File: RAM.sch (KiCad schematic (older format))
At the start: 3 parts, among them U2 MT41K64M16TW-107_AAT_J_TR

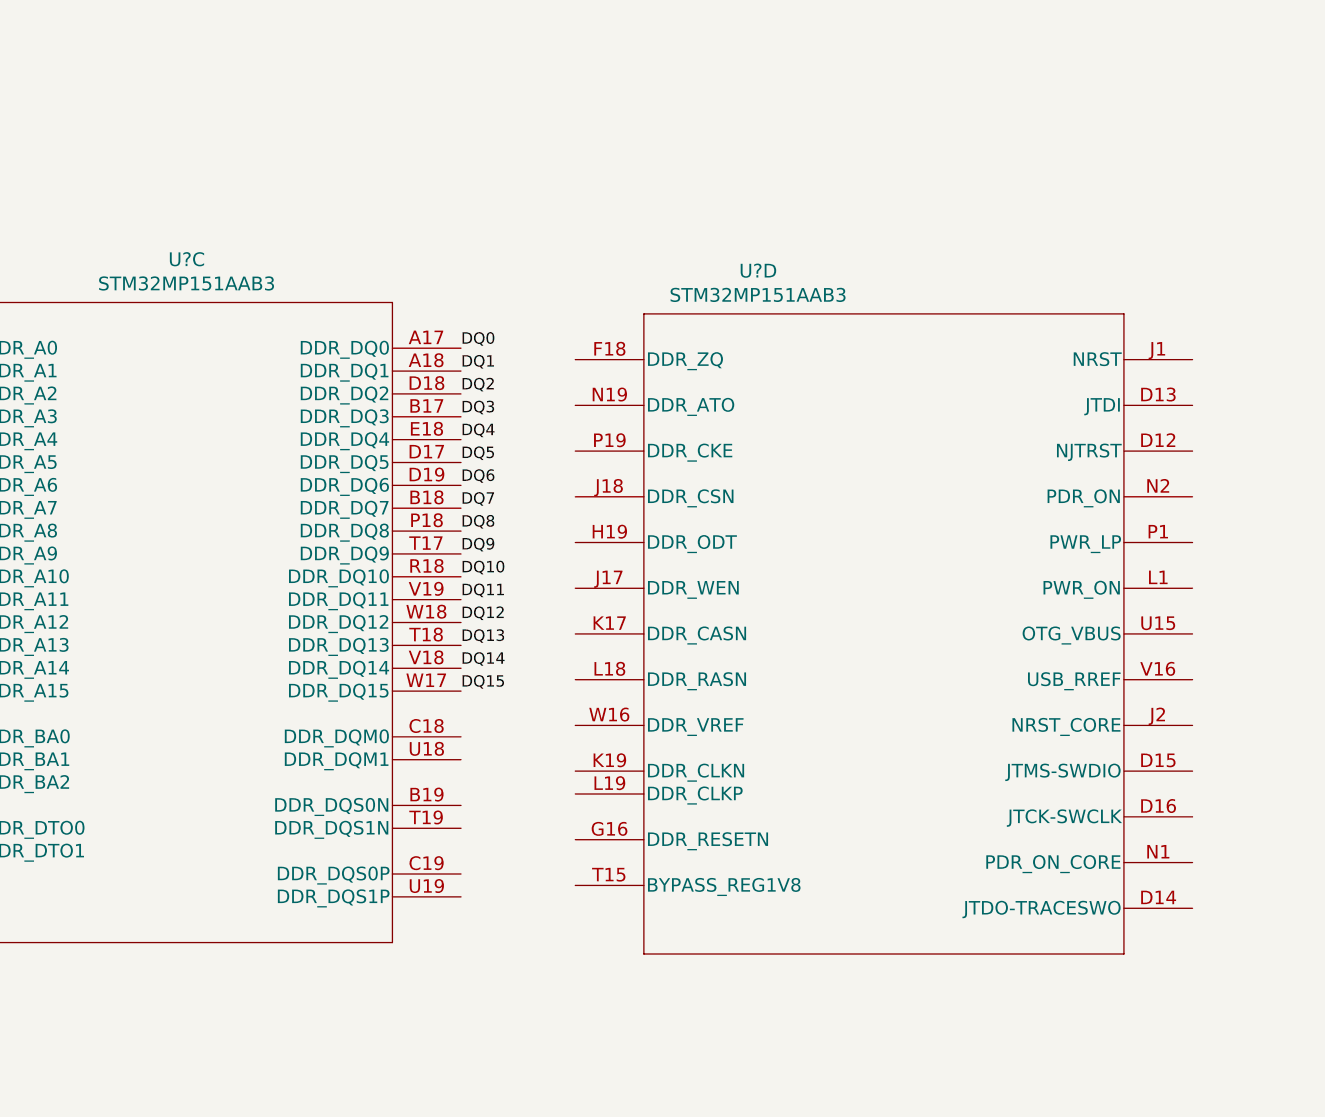
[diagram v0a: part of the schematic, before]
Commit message: Add bulk labels for RAM and ethernet
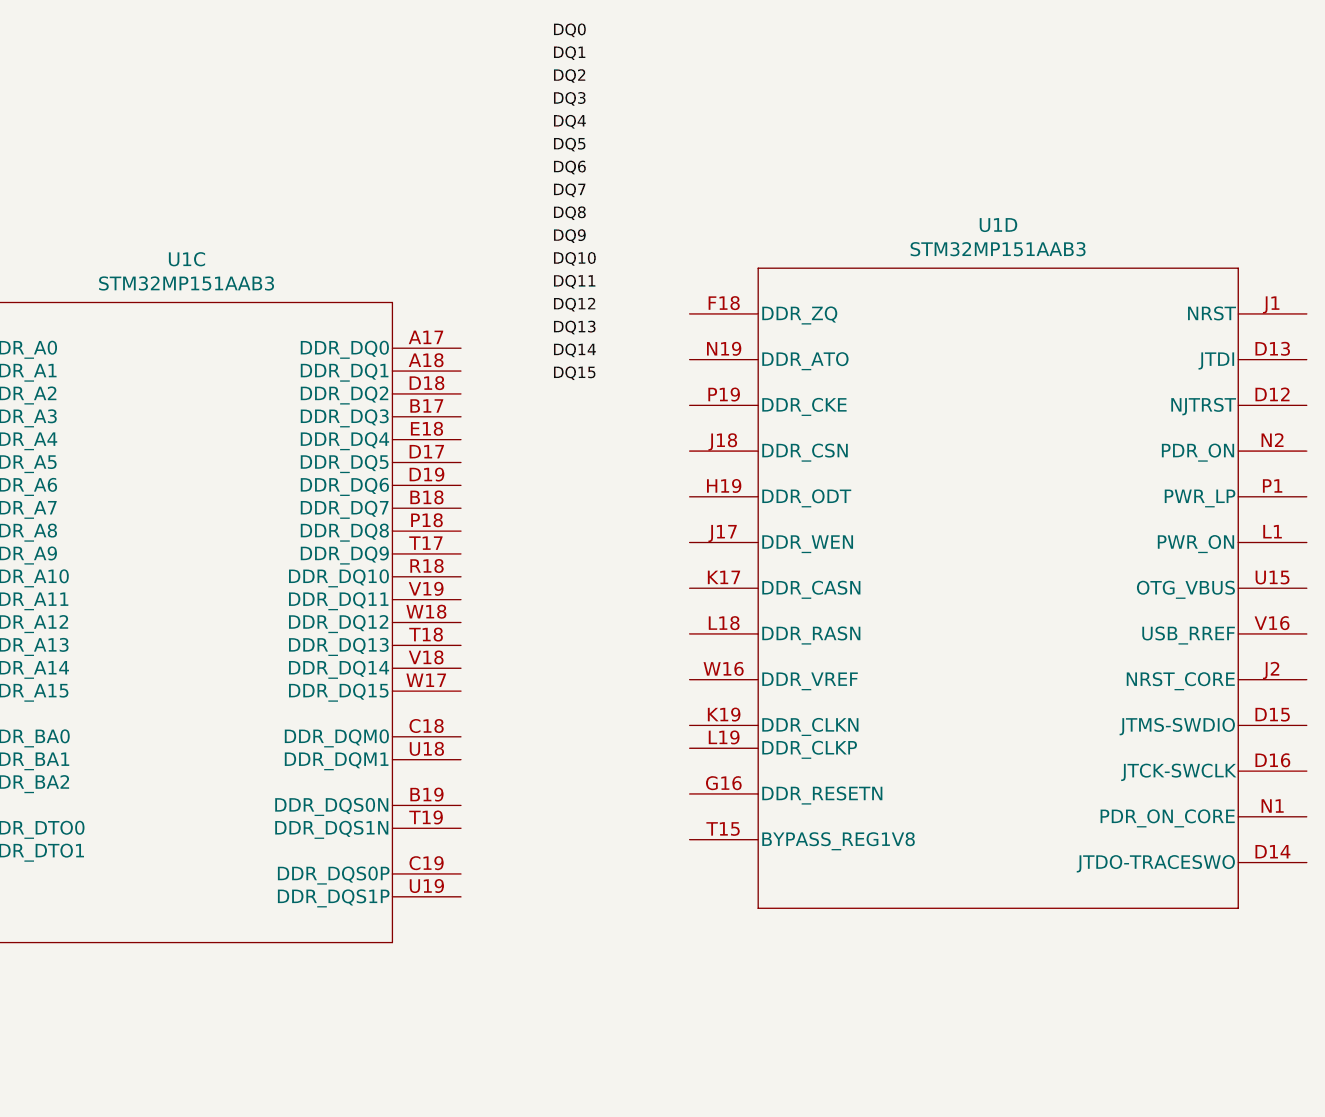
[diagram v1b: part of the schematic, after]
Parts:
- gave numbers to parts that had none: 1
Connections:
- net DQ0: no longer U1.A17 (DDR_DQ0)
- net DQ1: no longer U1.A18 (DDR_DQ1)
- net DQ10: no longer U1.R18 (DDR_DQ10)
- net DQ11: no longer U1.V19 (DDR_DQ11)
- net DQ12: no longer U1.W18 (DDR_DQ12)
- net DQ13: no longer U1.T18 (DDR_DQ13)
- net DQ14: no longer U1.V18 (DDR_DQ14)
- net DQ15: no longer U1.W17 (DDR_DQ15)
- net DQ2: no longer U1.D18 (DDR_DQ2)
- net DQ3: no longer U1.B17 (DDR_DQ3)
- net DQ4: no longer U1.E18 (DDR_DQ4)
- net DQ5: no longer U1.D17 (DDR_DQ5)
- net DQ6: no longer U1.D19 (DDR_DQ6)
- net DQ7: no longer U1.B18 (DDR_DQ7)
- net DQ8: no longer U1.P18 (DDR_DQ8)
- net DQ9: no longer U1.T17 (DDR_DQ9)
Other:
- moved on the sheet: U1D
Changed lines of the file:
@@
 L LinuxBoard:STM32MP151AAB3 U?
 U 4 1 6049E2E1
-P 7350 1450
+P 7850 1250
 AR Path="/601728E9/6049E2E1" Ref="U?"  Part="4"
-AR Path="/60172A77/6049E2E1" Ref="U?"  Part="4"
-F 0 "U?" H 8650 1837 60  0000 C CNN
-F 1 "STM32MP151AAB3" H 8650 1731 60  0000 C CNN
-F 2 "LinuxBoard:STM32MP151AAB3" H 8350 1690 60  0001 C CNN
-F 3 "" H 7350 1450 60  0000 C CNN
-	4    7350 1450
+AR Path="/60172A77/6049E2E1" Ref="U1"  Part="4"
+F 0 "U1" H 9700 1637 60  0000 C CNN
+F 1 "STM32MP151AAB3" H 9700 1531 60  0000 C CNN
+F 2 "LinuxBoard:STM32MP151AAB3" H 8850 1490 60  0001 C CNN
+F 3 "" H 7850 1250 60  0000 C CNN
+	4    7850 1250
 	1    0    0    -1
 $EndComp
@@
 P 4950 1400
 AR Path="/601728E9/6049E2E7" Ref="U?"  Part="3"
-AR Path="/60172A77/6049E2E7" Ref="U?"  Part="3"
-F 0 "U?" H 6150 1787 60  0000 C CNN
+AR Path="/60172A77/6049E2E7" Ref="U1"  Part="3"
+F 0 "U1" H 6150 1787 60  0000 C CNN
 F 1 "STM32MP151AAB3" H 6150 1681 60  0000 C CNN
 F 2 "LinuxBoard:STM32MP151AAB3" H 5950 1640 60  0001 C CNN
@@
 	1350 7100 1350 7200
 $Comp
-L power:GND #PWR?
+L power:GND #PWR011
 U 1 1 60844341
 P 1350 7200
-F 0 "#PWR?" H 1350 6950 50  0001 C CNN
+F 0 "#PWR011" H 1350 6950 50  0001 C CNN
 F 1 "GND" H 1355 7027 50  0000 C CNN
 F 2 "" H 1350 7200 50  0001 C CNN
@@
 Text Label 4950 1400 2    50   ~ 0
 A0
-Text Label 7350 2900 0    50   ~ 0
+Text Label 7750 1550 0    50   ~ 0
 DQ15
-Text Label 7350 2800 0    50   ~ 0
+Text Label 7750 1450 0    50   ~ 0
 DQ14
-Text Label 7350 2700 0    50   ~ 0
+Text Label 7750 1350 0    50   ~ 0
 DQ13
-Text Label 7350 2600 0    50   ~ 0
+Text Label 7750 1250 0    50   ~ 0
 DQ12
-Text Label 7350 2500 0    50   ~ 0
+Text Label 7750 1150 0    50   ~ 0
 DQ11
-Text Label 7350 2400 0    50   ~ 0
+Text Label 7750 1050 0    50   ~ 0
 DQ10
-Text Label 7350 2300 0    50   ~ 0
+Text Label 7750 950  0    50   ~ 0
 DQ9
-Text Label 7350 2200 0    50   ~ 0
+Text Label 7750 850  0    50   ~ 0
 DQ8
-Text Label 7350 2100 0    50   ~ 0
+Text Label 7750 750  0    50   ~ 0
 DQ7
-Text Label 7350 2000 0    50   ~ 0
+Text Label 7750 650  0    50   ~ 0
 DQ6
-Text Label 7350 1900 0    50   ~ 0
+Text Label 7750 550  0    50   ~ 0
 DQ5
-Text Label 7350 1800 0    50   ~ 0
+Text Label 7750 450  0    50   ~ 0
 DQ4
-Text Label 7350 1700 0    50   ~ 0
+Text Label 7750 350  0    50   ~ 0
 DQ3
-Text Label 7350 1600 0    50   ~ 0
+Text Label 7750 250  0    50   ~ 0
 DQ2
-Text Label 7350 1500 0    50   ~ 0
+Text Label 7750 150  0    50   ~ 0
 DQ1
-Text Label 7350 1400 0    50   ~ 0
+Text Label 7750 50   0    50   ~ 0
 DQ0
 Text Label 1000 5900 2    50   ~ 0
@@
 	1000 7100 1000 7200
 $Comp
-L power:GND #PWR?
+L power:GND #PWR010
 U 1 1 60E94F4D
 P 1000 7200
-F 0 "#PWR?" H 1000 6950 50  0001 C CNN
+F 0 "#PWR010" H 1000 6950 50  0001 C CNN
 F 1 "GND" H 1005 7027 50  0000 C CNN
 F 2 "" H 1000 7200 50  0001 C CNN

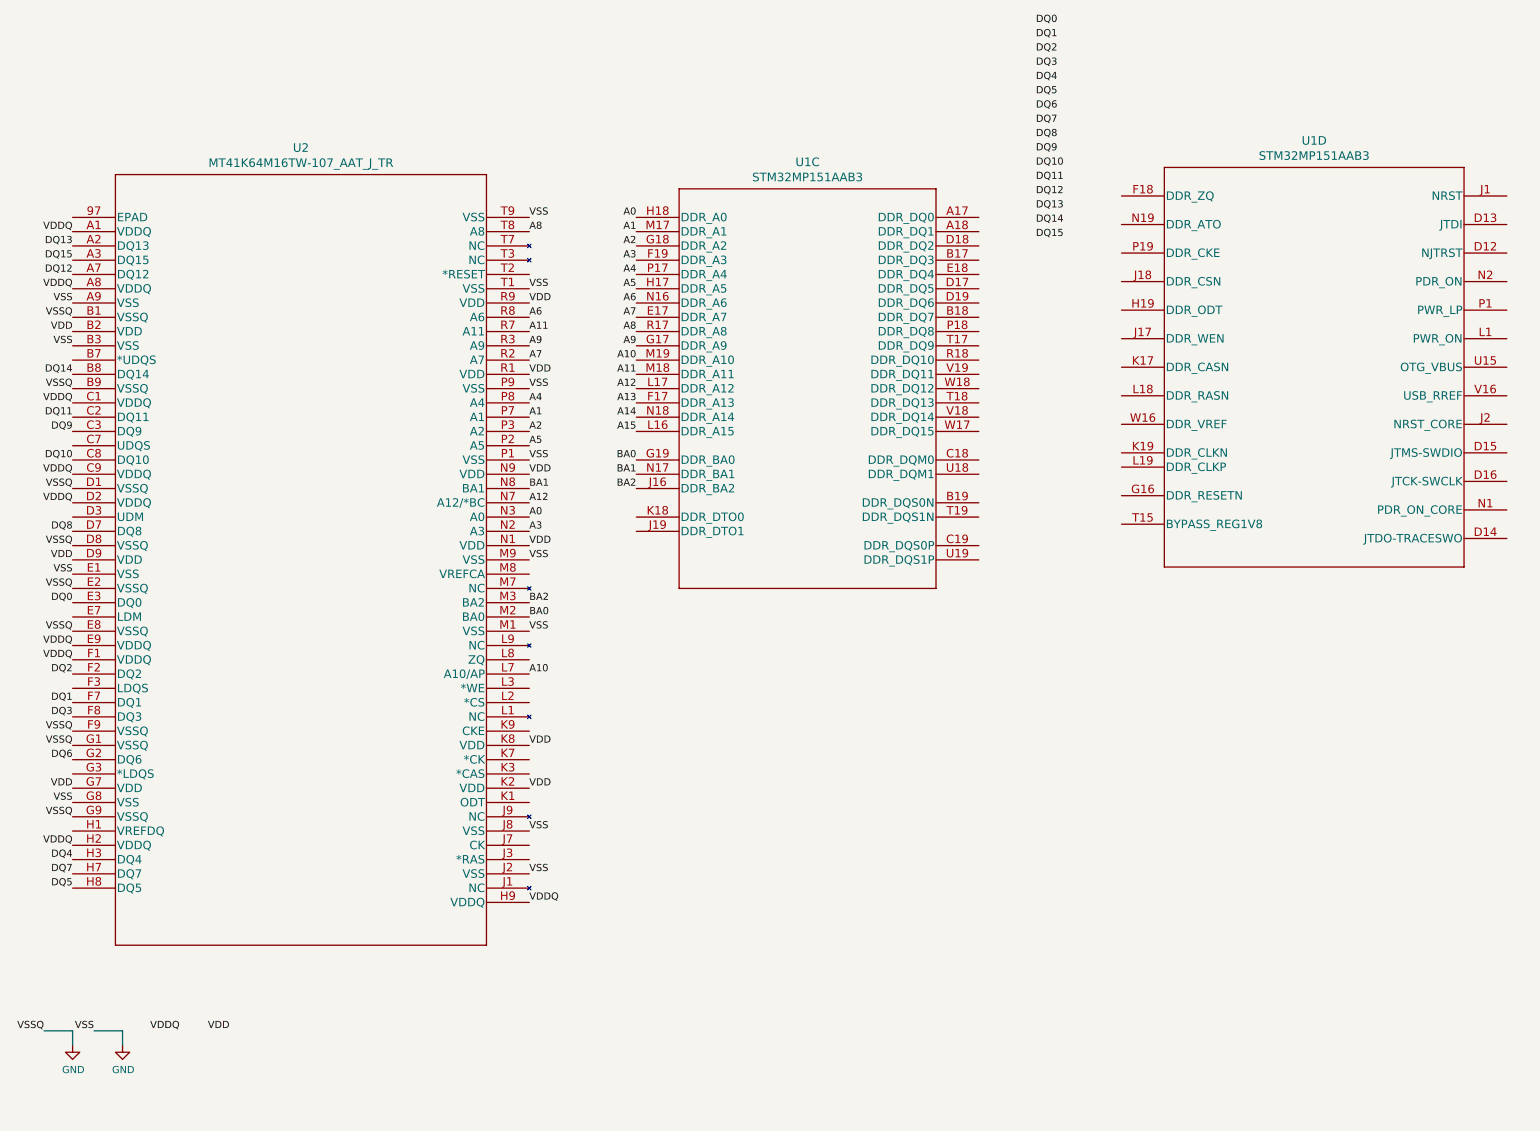
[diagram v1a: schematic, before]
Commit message: Complete ethernet and PMIC circuitry
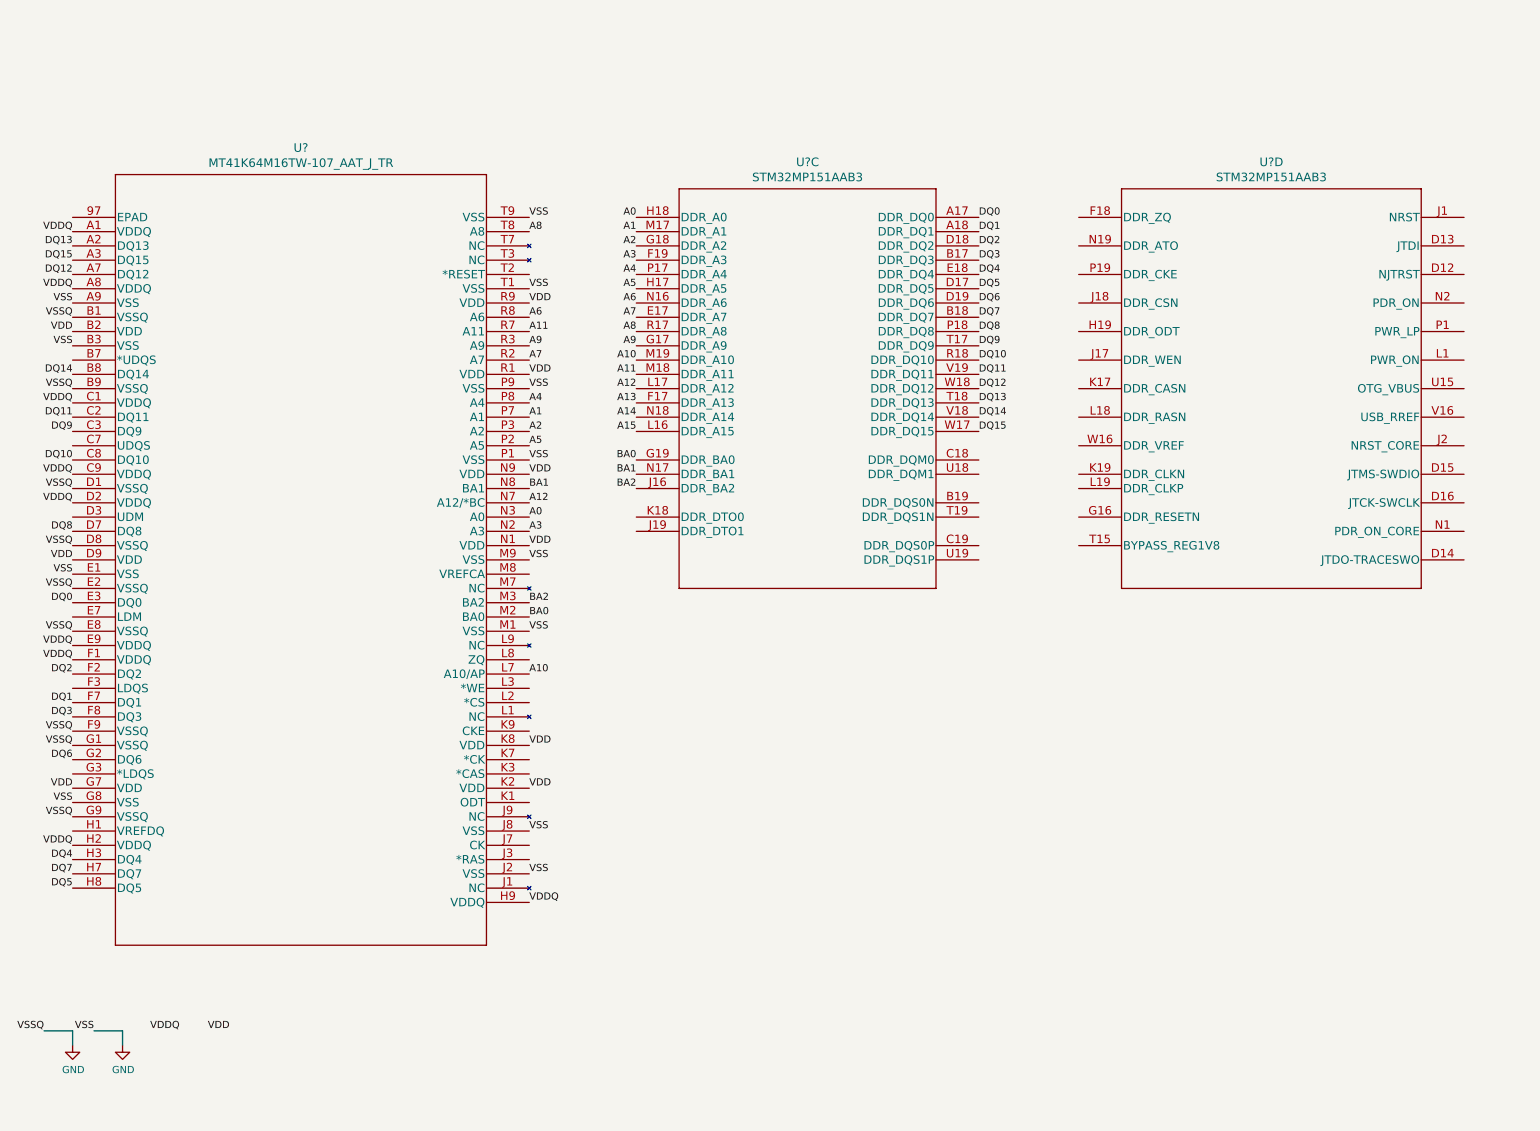
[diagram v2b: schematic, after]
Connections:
- net DQ0: now also U1.A17 (DDR_DQ0)
- net DQ1: now also U1.A18 (DDR_DQ1)
- net DQ10: now also U1.R18 (DDR_DQ10)
- net DQ11: now also U1.V19 (DDR_DQ11)
- net DQ12: now also U1.W18 (DDR_DQ12)
- net DQ13: now also U1.T18 (DDR_DQ13)
- net DQ14: now also U1.V18 (DDR_DQ14)
- net DQ15: now also U1.W17 (DDR_DQ15)
- net DQ2: now also U1.D18 (DDR_DQ2)
- net DQ3: now also U1.B17 (DDR_DQ3)
- net DQ4: now also U1.E18 (DDR_DQ4)
- net DQ5: now also U1.D17 (DDR_DQ5)
- net DQ6: now also U1.D19 (DDR_DQ6)
- net DQ7: now also U1.B18 (DDR_DQ7)
- net DQ8: now also U1.P18 (DDR_DQ8)
- net DQ9: now also U1.T17 (DDR_DQ9)
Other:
- moved on the sheet: U?D
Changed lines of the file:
@@
 U 1 1 60175F93
 P 1000 1400
-F 0 "U2" H 2600 1887 60  0000 C CNN
+F 0 "U?" H 2600 1887 60  0000 C CNN
 F 1 "MT41K64M16TW-107_AAT_J_TR" H 2600 1781 60  0000 C CNN
 F 2 "LinuxBoard:MT41K64M16TW-107_AAT_J_TR" H 2600 1740 60  0001 C CNN
@@
 L LinuxBoard:STM32MP151AAB3 U?
 U 4 1 6049E2E1
-P 7850 1250
+P 7550 1400
 AR Path="/601728E9/6049E2E1" Ref="U?"  Part="4"
 AR Path="/60172A77/6049E2E1" Ref="U1"  Part="4"
-F 0 "U1" H 9700 1637 60  0000 C CNN
-F 1 "STM32MP151AAB3" H 9700 1531 60  0000 C CNN
-F 2 "LinuxBoard:STM32MP151AAB3" H 8850 1490 60  0001 C CNN
-F 3 "" H 7850 1250 60  0000 C CNN
-	4    7850 1250
+F 0 "U?" H 9400 1787 60  0000 C CNN
+F 1 "STM32MP151AAB3" H 9400 1681 60  0000 C CNN
+F 2 "LinuxBoard:STM32MP151AAB3" H 8550 1640 60  0001 C CNN
+F 3 "" H 7550 1400 60  0000 C CNN
+	4    7550 1400
 	1    0    0    -1
 $EndComp
@@
 AR Path="/601728E9/6049E2E7" Ref="U?"  Part="3"
 AR Path="/60172A77/6049E2E7" Ref="U1"  Part="3"
-F 0 "U1" H 6150 1787 60  0000 C CNN
+F 0 "U?" H 6150 1787 60  0000 C CNN
 F 1 "STM32MP151AAB3" H 6150 1681 60  0000 C CNN
 F 2 "LinuxBoard:STM32MP151AAB3" H 5950 1640 60  0001 C CNN
@@
 U 1 1 60844341
 P 1350 7200
-F 0 "#PWR011" H 1350 6950 50  0001 C CNN
+F 0 "#PWR?" H 1350 6950 50  0001 C CNN
 F 1 "GND" H 1355 7027 50  0000 C CNN
 F 2 "" H 1350 7200 50  0001 C CNN
@@
 Text Label 4950 1400 2    50   ~ 0
 A0
-Text Label 7750 1550 0    50   ~ 0
+Text Label 7350 2900 0    50   ~ 0
 DQ15
-Text Label 7750 1450 0    50   ~ 0
+Text Label 7350 2800 0    50   ~ 0
 DQ14
-Text Label 7750 1350 0    50   ~ 0
+Text Label 7350 2700 0    50   ~ 0
 DQ13
-Text Label 7750 1250 0    50   ~ 0
+Text Label 7350 2600 0    50   ~ 0
 DQ12
-Text Label 7750 1150 0    50   ~ 0
+Text Label 7350 2500 0    50   ~ 0
 DQ11
-Text Label 7750 1050 0    50   ~ 0
+Text Label 7350 2400 0    50   ~ 0
 DQ10
-Text Label 7750 950  0    50   ~ 0
+Text Label 7350 2300 0    50   ~ 0
 DQ9
-Text Label 7750 850  0    50   ~ 0
+Text Label 7350 2200 0    50   ~ 0
 DQ8
-Text Label 7750 750  0    50   ~ 0
+Text Label 7350 2100 0    50   ~ 0
 DQ7
-Text Label 7750 650  0    50   ~ 0
+Text Label 7350 2000 0    50   ~ 0
 DQ6
-Text Label 7750 550  0    50   ~ 0
+Text Label 7350 1900 0    50   ~ 0
 DQ5
-Text Label 7750 450  0    50   ~ 0
+Text Label 7350 1800 0    50   ~ 0
 DQ4
-Text Label 7750 350  0    50   ~ 0
+Text Label 7350 1700 0    50   ~ 0
 DQ3
-Text Label 7750 250  0    50   ~ 0
+Text Label 7350 1600 0    50   ~ 0
 DQ2
-Text Label 7750 150  0    50   ~ 0
+Text Label 7350 1500 0    50   ~ 0
 DQ1
-Text Label 7750 50   0    50   ~ 0
+Text Label 7350 1400 0    50   ~ 0
 DQ0
 Text Label 1000 5900 2    50   ~ 0
@@
 U 1 1 60E94F4D
 P 1000 7200
-F 0 "#PWR010" H 1000 6950 50  0001 C CNN
+F 0 "#PWR?" H 1000 6950 50  0001 C CNN
 F 1 "GND" H 1005 7027 50  0000 C CNN
 F 2 "" H 1000 7200 50  0001 C CNN
